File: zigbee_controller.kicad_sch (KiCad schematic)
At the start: 59 parts, among them J1 +24V, J10 IO23 load, J11 IO20 load, J12 IO22 load, J13 IO21 load, J2 5v, J3 Conn_01x06, J4 Conn_01x07, J5 Conn_01x05, P1 USB_C_Plug_USB2.0, Q2 IRLB3813, Q3 IRLB3813, Q4 IRLB3813, Q5 IRLB3813, SW2 EN, SW4 Boot, U1 TPS54560, U2 ESP32-C6-MINI-1, U3 AMS1117-3.3, U4 TC4427xOA, U5 TC4427xOA

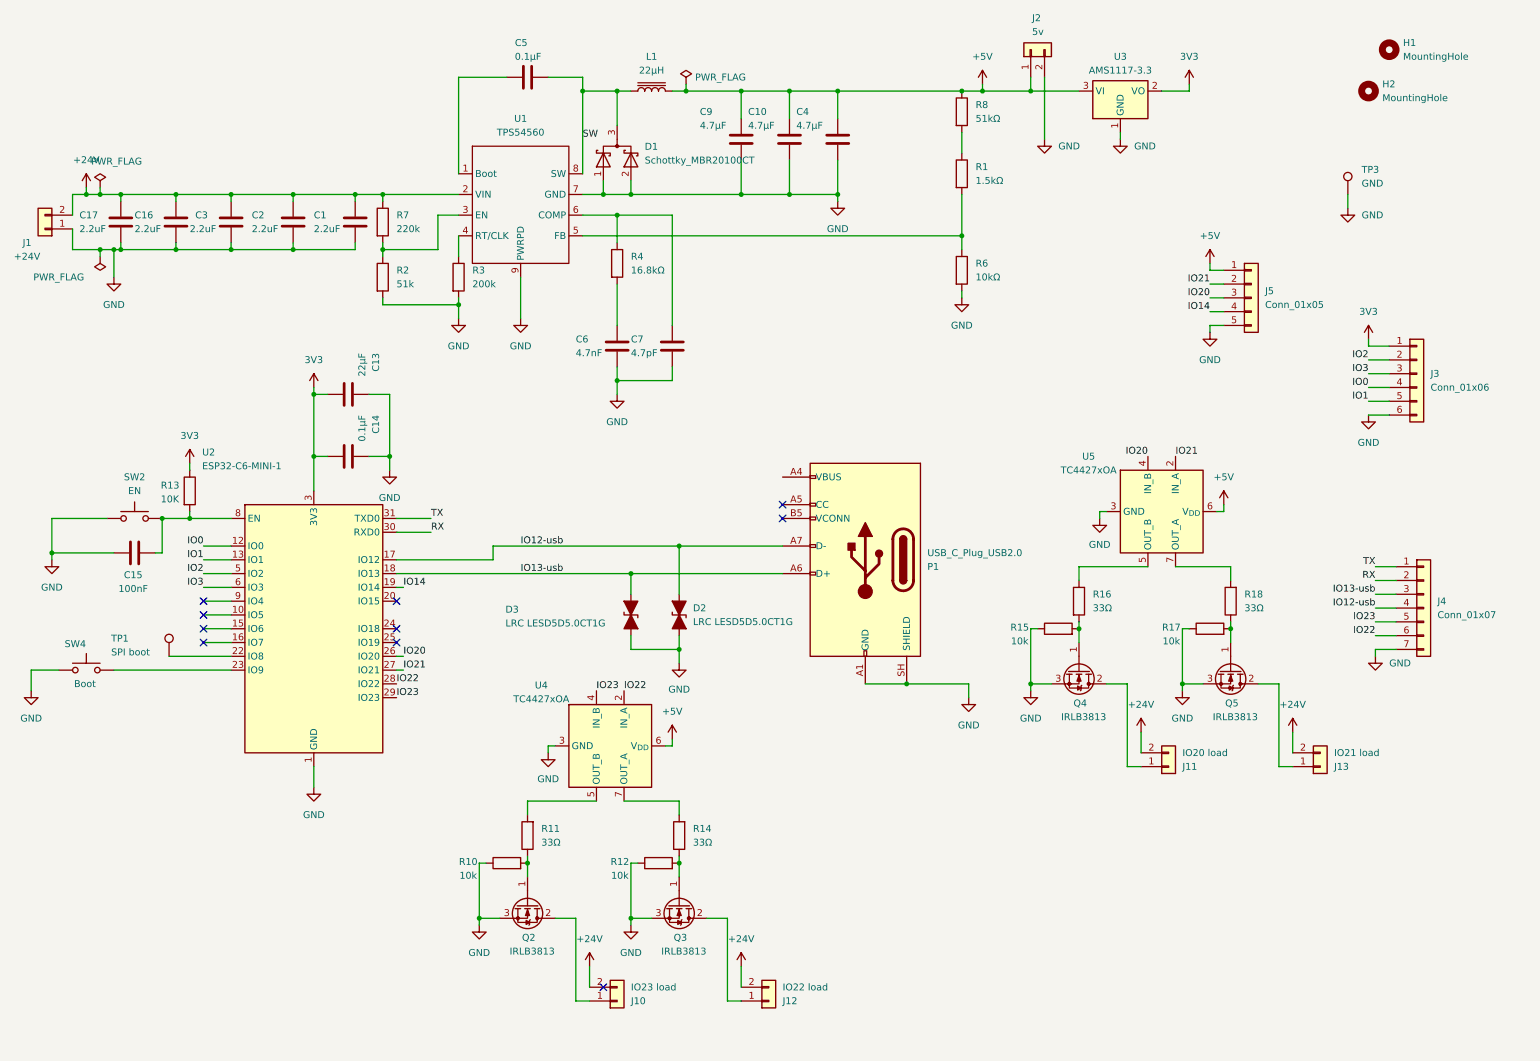
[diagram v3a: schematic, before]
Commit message: before making space for heatsink
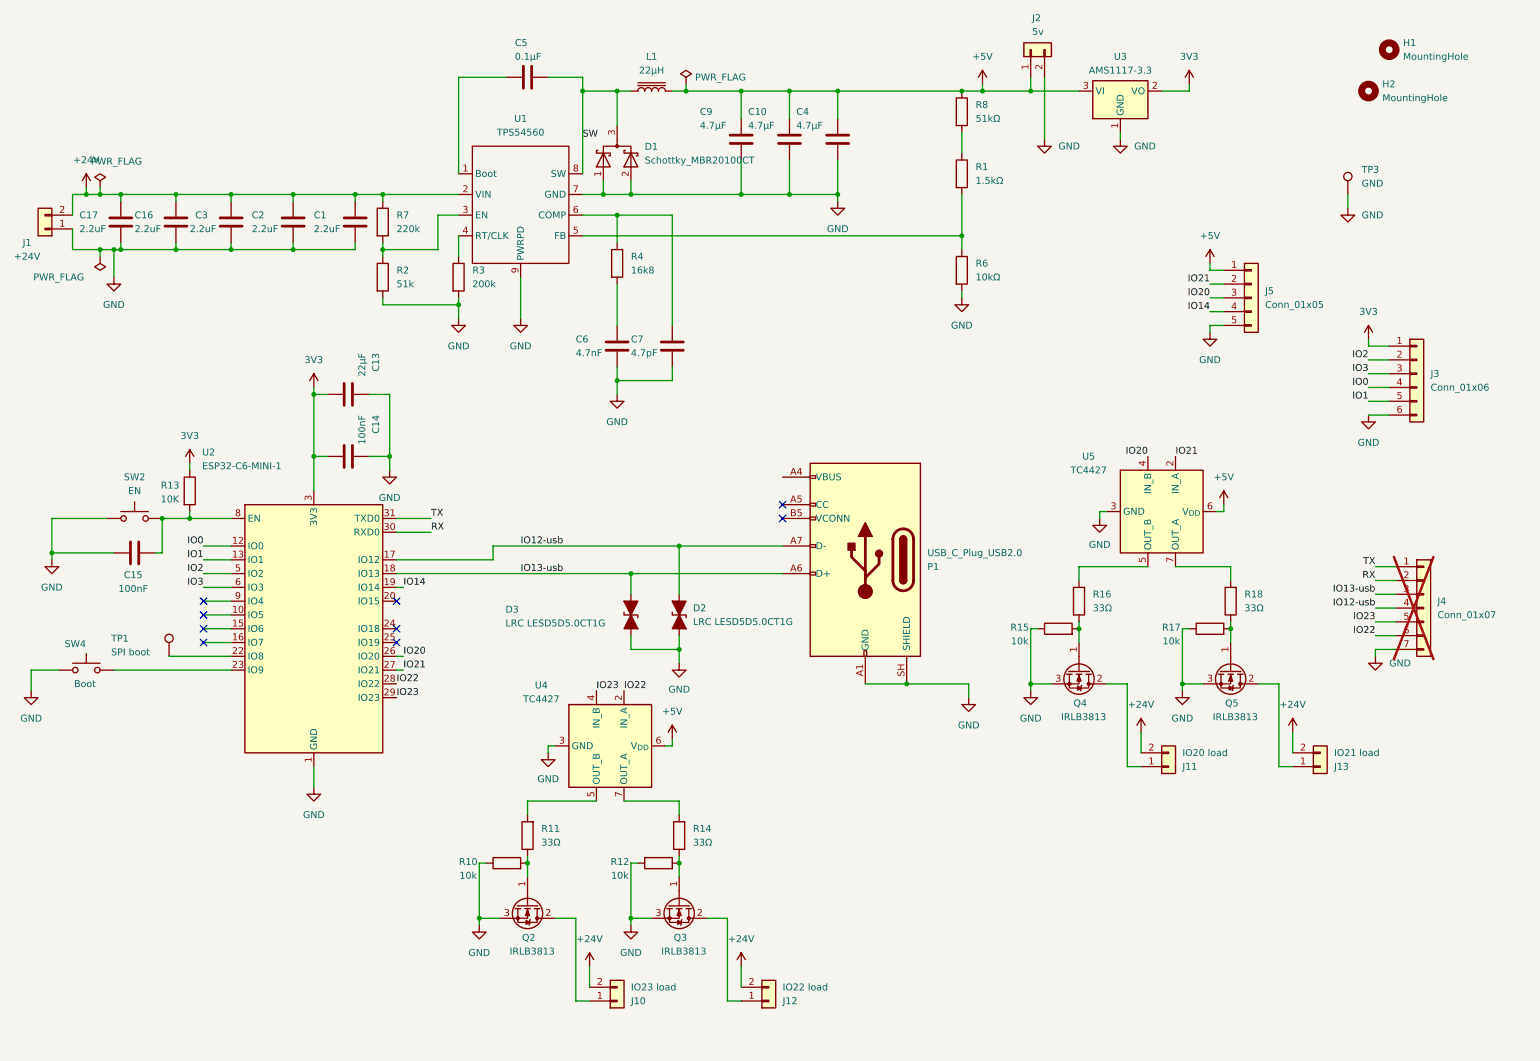
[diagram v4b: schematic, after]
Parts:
- C14: value 0.1μF -> 100nF
- J4: now not fitted
- L1: footprint Inductor_SMD:L_Bourns-SRN8040_8x8.15mm -> Inductor_SMD:L_Chilisin_BMRF00101040; ALI (none) -> https://pt.aliexpress.com/item/1005007254030376.html?spm=a2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
- R4: value 16.8kΩ -> 16k8
- U4, U5: value TC4427xOA -> TC4427
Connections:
- no-connect marks 10 -> 9
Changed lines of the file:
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@@
 	)
 	(no_connect
-		(at 119.38 193.04)
-	)
-	(no_connect
 		(at 45.72 127)
 	)
@@
 		(on_board yes)
 		(in_pos_files yes)
-		(dnp no)
+		(dnp yes)
 		(property "Reference" "J4"
 			(at 273.05 121.9199 0)
@@
 			)
 		)
-		(property "Value" "0.1μF"
+		(property "Value" "100nF"
 			(at 74.93 87.63 0)
 			(show_name no)
@@
 			)
 		)
-		(property "Value" "16.8kΩ"
+		(property "Value" "16k8"
 			(at 124.46 60.9599 0)
 			(show_name no)
@@
 			)
 		)
-		(property "Value" "TC4427xOA"
+		(property "Value" "TC4427"
 			(at 208.788 97.79 90)
 			(show_name no)
@@
 			)
 		)
-		(property "Footprint" "Inductor_SMD:L_Bourns-SRN8040_8x8.15mm"
+		(property "Footprint" "Inductor_SMD:L_Chilisin_BMRF00101040"
 			(at 128.27 27.94 0)
 			(hide yes)
@@
 			)
 		)
+		(property "ALI" "https://pt.aliexpress.com/item/1005007254030376.html?spm=a2g0o.productlist.main.8.18d64an84an8NG&algo_pvid=63a61315-a6b1-462a-9664-1cc09ba9c9ee&aem_p4p_detail=202604211447301858219910874370000274182&algo_exp_id=63a61315-a6b1-462a-9664-1cc09ba9c9ee-7&pdp_ext_f=%7B%22order%22%3A%22344%22%2C%22spu_best_type%22%3A%22price%22%2C%22eval%22%3A%221%22%2C%22fromPage%22%3A%22search%22%7D&pdp_npi=6%40dis%21BRL%2120.52%2120.52%21%21%2126.04%2126.04%21%40210328c017768080498948779e2bee%2112000039958467827%21sea%21BR%21715047753%21X%211%210%21n_tag%3A-29919%3Bd%3Aa4e9d9bc%3Bm03_new_user%3A-29895&curPageLogUid=OCu73UCZnwux&utparam-url=scene%3Asearch%7Cquery_from%3A%7Cx_object_id%3A1005007254030376%7C_p_origin_prod%3A&search_p4p_id=202604211447301858219910874370000274182_2"
+			(at 128.27 27.94 90)
+			(hide yes)
+			(show_name no)
+			(do_not_autoplace no)
+			(effects
+				(font
+					(size 1.27 1.27)
+				)
+			)
+		)
 		(pin "1"
 		)
@@
 			)
 		)
-		(property "Value" "TC4427xOA"
+		(property "Value" "TC4427"
 			(at 107.95 139.954 90)
 			(show_name no)
@@
 		)
 	)
+	(group ""
+		(members "00ef8aa2-176f-4130-bbe9-788788138131" "0c69c121-a8a0-4c9a-8b2b-4cf9b0dab46e"
+			"0cb81708-3309-44e1-bc4c-f4874eb2cbc2" "0d3e182c-18c9-483f-8e0a-0056c6e06815"
+			"0d74f3a5-eb9c-4425-8b51-088296ffb3b9" "11bc4dbb-0893-46aa-86c2-ce7a2b8e4c2e"
+			"16b7ffb8-614e-47f3-94ed-63de18540853" "16c8a39e-c848-4991-b18f-164b93d5012f"
+			"170159fd-4069-45f5-b88a-6cb8c85c9ab1" "1825008e-681a-4186-856d-5cc8aa834c2f"
+			"19096a07-ad12-485f-87e6-b9d4b83f6f28" "1b8d8305-56af-4f06-b706-2a94093e2c9b"
+			"1b9753b4-554b-4307-8c7f-7805624ce736" "1d25ca7f-2703-4001-8558-957bc0821f26"
+			"1e8709f2-2d50-4330-a0d3-6cd1d280860f" "1e98da45-c1d5-4ae5-a0fc-cbb8e3d55e8e"
+			"205ec2b8-be09-4b96-a4ca-7b6abf17e089" "22868da6-9e97-4105-87f7-1cf1aa30c2c2"
+			"23522209-7930-4f12-b3b3-f9b929c2c0a2" "2475ad0e-8fcb-46e2-8b2b-bf4cc111c19e"
+			"24d9e66f-19b7-489c-ad29-0e5f46ea71bd" "24e0257b-7bd6-423e-a2b9-cdadd785738a"
+			"27f51bee-280e-44b6-83a5-66eecb7ea94d" "2823f51f-40f7-4632-b994-192965936578"
+			"291e06bc-6f99-462f-96d7-f263d04362d4" "2abbef87-a15d-4269-bec1-96cc22601fa2"
+			"2ca4a27b-fc05-4f6f-b433-4f44aaceaad6" "2efc59b9-1eba-4bfa-93e8-a9f3bc7e101b"
+			"2f64733e-1b2c-4725-8d42-8fddda4cb43a" "30d67de4-5f7f-4852-9a22-c44a3bebfb40"
+			"32040ff5-857e-4036-b6c7-2eae787d98ea" "32107fd9-14e2-465c-aa5b-2ab5b1a8d604"
+			"359c0df0-9187-472d-830b-eb0e4b56a01d" "3604fe73-3e7e-4d8c-9052-5e15dace96aa"
+			"376d6545-fae6-4fb3-9d48-2843365d77ce" "393ae429-135c-4e3e-86e3-cc2cf12f49e8"
+			"39794c0d-c614-4c12-b4e9-afef67cc0e59" "3ae3b833-e0d2-4c9b-bcb4-ae9969d73db3"
+			"3c429a5c-1f8c-4958-9085-dbb5334cb8ab" "3c4702f1-285b-406a-b579-7fba264822f4"
+			"3d17fc58-9116-49af-9d58-e6ea6531c3d2" "41275b0b-6267-4ed6-8cfb-103103581dd3"
+			"41a5d517-2b18-461b-bb38-84204afeabc0" "4323ddec-fcbb-414d-bc60-a374826c0b22"
+			"4662acbd-9b89-43f4-8920-1cf1da32fd91" "49cdf3b3-9528-4901-85b3-bc5cffb0152a"
+			"4a74262b-913d-402d-8e57-6bc807178dd3" "4b51df57-7cf3-4fca-81e2-88b63b68140a"
+			"4d4e16e6-3d43-40db-8694-ba7849f79cab" "4f783318-3851-4e39-96aa-2c9d7597610e"
+			"5131cf46-d23c-41aa-ba69-aa15ca4b748e" "5254b13a-e5df-4355-bda6-abb30a3d7386"
+			"5275d6ac-584b-40f1-8e15-d93707cd91be" "559457ec-f4f7-432a-9ad2-99716797ae57"
+			"55d64d9f-b920-44fd-8d1a-d33763254af1" "58266d41-8262-4d2c-8e89-47a594561037"
+			"5d3360b5-6f13-4074-839e-b842a88d699b" "614c3105-482c-4773-9716-a01b476ea010"
+			"616f3177-b9b0-44bb-a30f-a246a3a9ad18" "62a621e2-196e-49fe-a2dc-04003a3a8868"
+			"63a7544d-84c9-45ae-8919-cf2de06927be" "64617598-29b5-4b94-af8c-06334d7082bb"
+			"65c20d66-ae4b-4be5-a06d-18f5466c4228" "672ad2db-60b6-4027-960c-2bd563c678c8"
+			"69e4687b-504c-448f-8b0f-3a22a5c0e48a" "6a999cfb-c089-4328-acae-ce8da364548b"
+			"6d42bae0-c332-4f3c-85e6-5751c803f4fa" "6fee591d-130d-4980-a2eb-388d59e64c52"
+			"73caed4c-d89e-408b-bcb4-e6d59a4f2267" "78b40dd6-f29b-46b9-bc3c-bf3bfee4b470"
+			"78cb1773-4776-4949-973d-0c10ff975984" "7bdd1370-37e1-4a46-86bd-23ac2c860b37"
+			"7d810b1a-1f62-4858-98a4-0cf53ac5a21e" "7f6c6605-41f0-4ed3-b6bf-d532a1e7d5ec"
+			"80bb56dc-e87d-42a0-97f9-51709edcb93a" "832b2a72-2ce8-4584-8e79-46a21adfa1a7"
+			"8335660f-3f10-4fdd-9c2d-350108056eeb" "851058d4-472c-402e-b18c-b4e9a9134c31"
+			"877f21ae-f420-468a-a917-b5fb6fefbf57" "878a5696-02cc-46fa-a732-96650e32d470"
+			"8857cb86-e42c-4bfe-b49f-2e0a58b23994" "8aac1dba-682a-4c74-a23c-c8dfbd82be4f"
+			"8b2931b2-c553-44aa-a694-ac1098a4fbfc" "8b91fa9f-7051-4c08-b66c-71cb50588cc0"
+			"8c6519f3-5b28-491d-90d5-9802159c9a34" "910ff9a4-1464-4341-99f2-99f5d817bce7"
+			"91153b03-15bb-4396-881d-ab21cbad5b8d" "935725a9-e1bb-449a-a118-98f2a48b94c9"
+			"939bcf85-f34a-459f-9f99-a8933fc23e35" "964e5137-2b69-4c61-aaf2-19572c8c9a69"
+			"96f40778-f3ed-4d7c-9f22-95517effcb69" "9974df2b-5ae9-4f33-a583-72e14771cc93"
+			"997b2de3-cb2e-48e5-b09a-6ec2158f7390" "9a9849dc-2aec-4af4-8067-5e2daef89dca"
+			"9b13759f-f8e0-48c6-bd1e-49348b4cd07b" "9c18e026-4721-47aa-be5b-17152b930499"
+			"9c7d0af0-bd14-44da-becb-14f996684f9d" "9ceb9431-6439-408d-99ad-926c5a0985f0"
+			"9f5c8a91-6892-4281-8840-ab0a76e20048" "a1ef9ddd-2674-4040-a9f2-b1b3cfe59963"
+			"a42e273e-400e-4d73-8478-6aac6567faed" "a4ca5434-204f-4a30-98dd-e2414e6aa6d6"
+			"a5a335ee-1906-40fc-babd-98e8dc94ccae" "a820b9f8-922b-4dce-a806-0db49862a384"
+			"a82c0bd5-43f9-4a71-b69e-ac86158acd89" "a9ce31e5-f5e7-4b43-b442-d8b6e2ba8890"
+			"ac431b2c-f7ea-4d35-8a04-5891a219b703" "af228157-85fd-491d-9faa-b9891f82ebf8"
+			"b06ad84a-5925-4d7a-b598-2033a96c92f4" "b8dca9cc-8253-4928-af67-b7af06897956"
+			"ba774e32-b882-4acb-b1de-86bc891ba7a6" "bbc5e02f-0dcd-47ae-b02b-98dd0e92139a"
+			"bd52a919-0b7b-42d9-9bcf-2800cc25e178" "bddca8b2-6fa2-4996-9ab1-363da94756e7"
+			"bf81eefc-dfb1-4ef1-bccc-2cde9ef36a32" "c2724638-839b-4cae-bd71-4692d46ee7c1"
+			"c4ab9468-c2f6-4b7a-ac75-5326684fb3b3" "c55869b3-7c8a-4ab8-a8c9-64925e73cb42"
+			"ca6aeab7-ec32-4766-8331-a0343c305c20" "cac4e678-ed8c-402b-8ca2-c42500ed8cb4"
+			"ceae6497-9193-4c85-b4ed-42ba2ccbd40c" "cf584716-7a72-45b8-b2b3-1ffe671e30de"
+			"d04046bc-0d14-4ab5-813d-df2f1ff28395" "d04d8dc5-e5e1-4cd2-9658-1c4abe024e89"
+			"d64f5836-4103-4a84-9dd5-1f7f0305f60e" "d73927b4-793d-4595-8aaf-50ea464e0738"
+			"d8c581fe-79b2-4249-9c5c-a3b900102f7f" "d8d73fd7-f6db-4287-bae5-9bba9eaf6b1e"
+			"d9a00c86-0de7-4ddd-a68a-25066c5bd9ec" "da15ab7c-eb15-4e17-a4e3-56534557d883"
+			"dc08dfb9-c5bd-45c4-a8fb-53c28003770e" "ddd026ea-917b-4a52-a031-e6b4d5327bea"
+			"dfa89d7a-d5d1-4cd8-b896-e67718d3610c" "e1a6d7ab-0efd-4aa1-adf1-03057288866c"
+			"e35ee571-f46b-4b87-a1c3-0a3f2f9596a3" "e4628858-0e6e-4a69-a8b4-1ce264ece58b"
+			"e5b303f7-efc8-4679-88e5-78bffac98948" "e5f0b49a-5184-4c1d-9574-c16d0ea13899"
+			"e6facc76-abca-4466-97d7-6cb08c2ec179" "ebaf8a70-b963-4010-b263-9d76f57274ac"
+			"edac970d-c8b3-4eaa-9821-65af29c8348b" "ee0fcfcf-1229-43bd-8195-c49866356447"
+			"ef082814-777d-4026-9888-3e4118f29c59" "ef2b584d-c974-4356-871a-d648bfebfa60"
+			"f18989f8-0bd1-4bf5-aea1-272fe228a9f6" "f302dbbc-7799-4432-97a7-2e4ff745fada"
+			"f3ca1fd3-6364-42b7-85d3-6b33ca17db2a" "f4004a81-67ee-496f-ba27-92ca1338b2fd"
+			"f8132236-eec2-4fb9-a06f-8c487b4fe1a0" "f907f5a7-56c1-42ae-bab1-210250c96c0f"
+			"faaca74b-823b-435c-92ce-e99667f9dcc3" "fc68a5ef-6011-4464-b696-76ab1fa512fa"
+			"fec0336b-d5bd-4d19-87ca-dfd0e88e1ba4" "ffb95fe5-0330-4aba-9656-be73aafe31a0"
+		)
+	)
